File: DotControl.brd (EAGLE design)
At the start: 30.7 x 65 mm, 21 parts, among them CN1 1X4-BIG, J3 USB-MICROB, SW2 Previous, SW5 Previous, SW6 Next, SW8 Ok, U1 ATMEGA328P-MU-QFN32

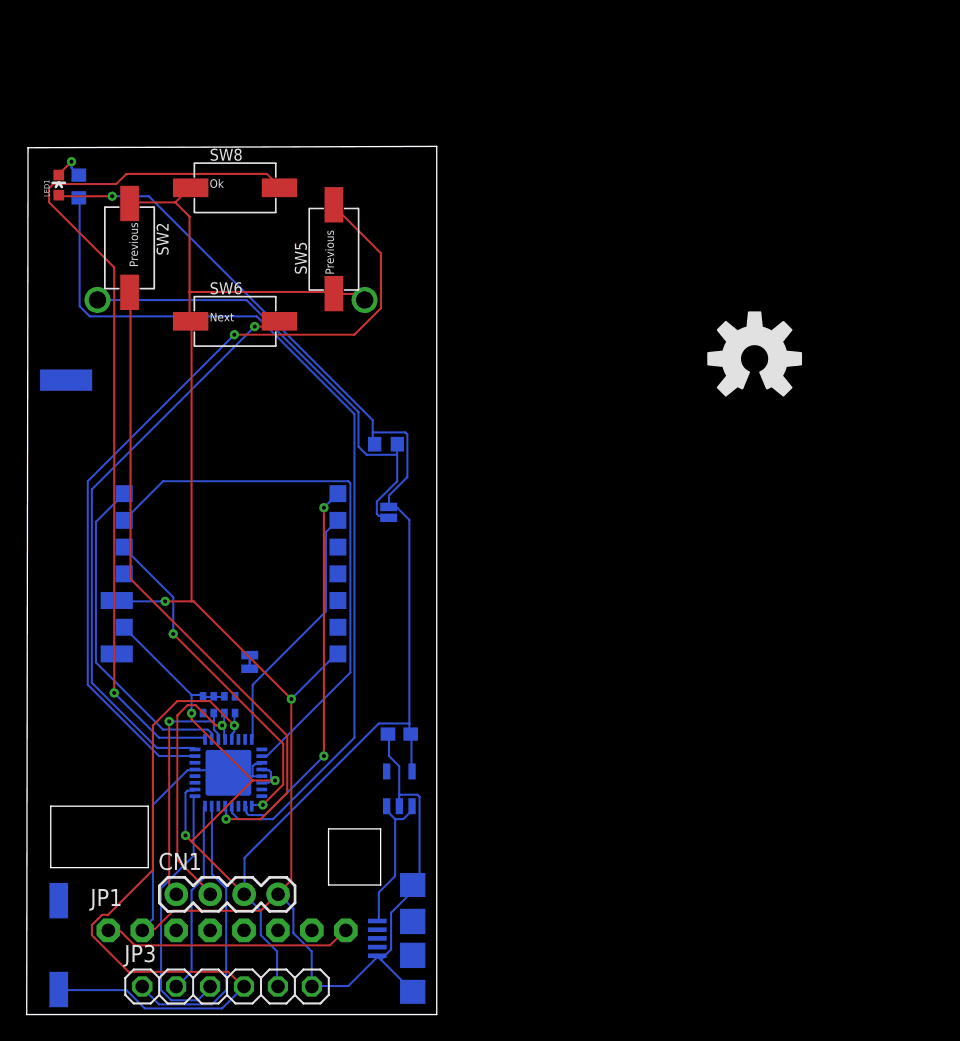
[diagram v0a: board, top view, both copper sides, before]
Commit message: Add RGB and crystal
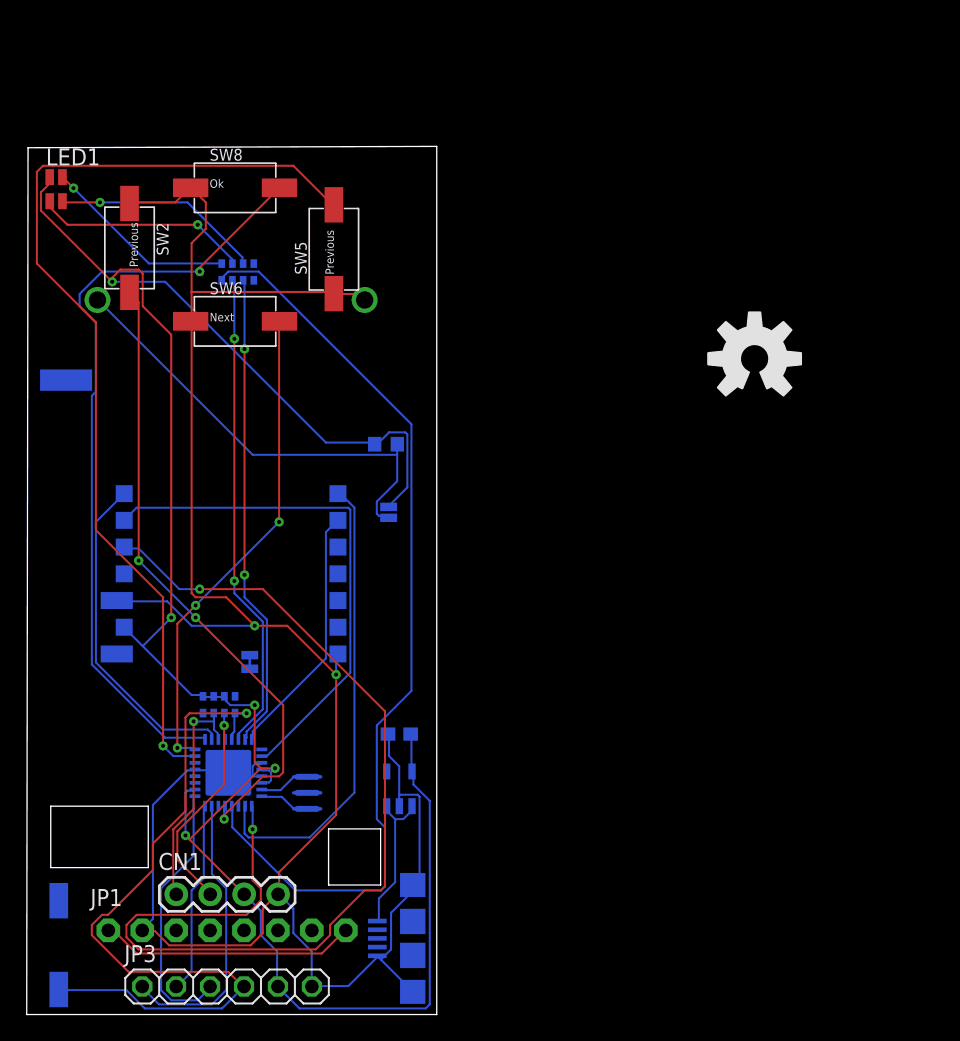
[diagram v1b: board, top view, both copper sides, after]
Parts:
- removed R1: (no value), resistor:R0603
- added R2: (no value), SparkFun:0603-ARV
- added Y1: (no value), SparkFun-Clocks:RESONATOR-SMD-3.2X1.3
- LED1: value (none) -> GM1WA55311A; device SparkFun:LED-0603 -> led:GM1WA55311A
- moved LED1 0.36 mm to (2.20, 61.8)
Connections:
- removed net N$1: LED1.C, R1.2
- new net N$10: LED1.2, R2.6
- new net N$15: LED1.1, R2.5
- new net N$6: U1.7, Y1.3
- new net N$8: U1.8, Y1.1
- new net N$9: LED1.3, R2.7
- net +3V3: now also LED1.4; no longer LED1.A
- net GND: now also Y1.2
- net LED: now also R2.4; no longer R1.1
- net RXD: now also R2.3
- net TXD: now also R2.2
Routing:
- net RSDI: track 25.7 -> 79.0 mm
- net RXD: track 0.00 -> 36.1 mm, vias 0 -> 2
- net TXD: track 0.00 -> 35.8 mm, vias 0 -> 2
- net +3V3: track 128.0 -> 156.2 mm, vias 4 -> 5
- net N$10: track 0.00 -> 16.1 mm, vias 0 -> 1
- net N$9: track 0.00 -> 15.7 mm, vias 0 -> 1
- net N$15: track 0.00 -> 14.6 mm, vias 0 -> 1
- net BUZZER: track 62.0 -> 73.2 mm
- net GND: track 155.3 -> 166.4 mm
- net MOVE_INT: track 66.2 -> 57.6 mm
- net OUTB: track 43.6 -> 36.5 mm, vias 1 -> 3
- net RSDO: track 28.3 -> 34.9 mm, vias 2 -> 0
- net SCL: track 20.9 -> 17.1 mm
- net N$6: track 0.00 -> 2.83 mm
- net RSCK: track 41.6 -> 38.8 mm
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
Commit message: Add strong GND plane
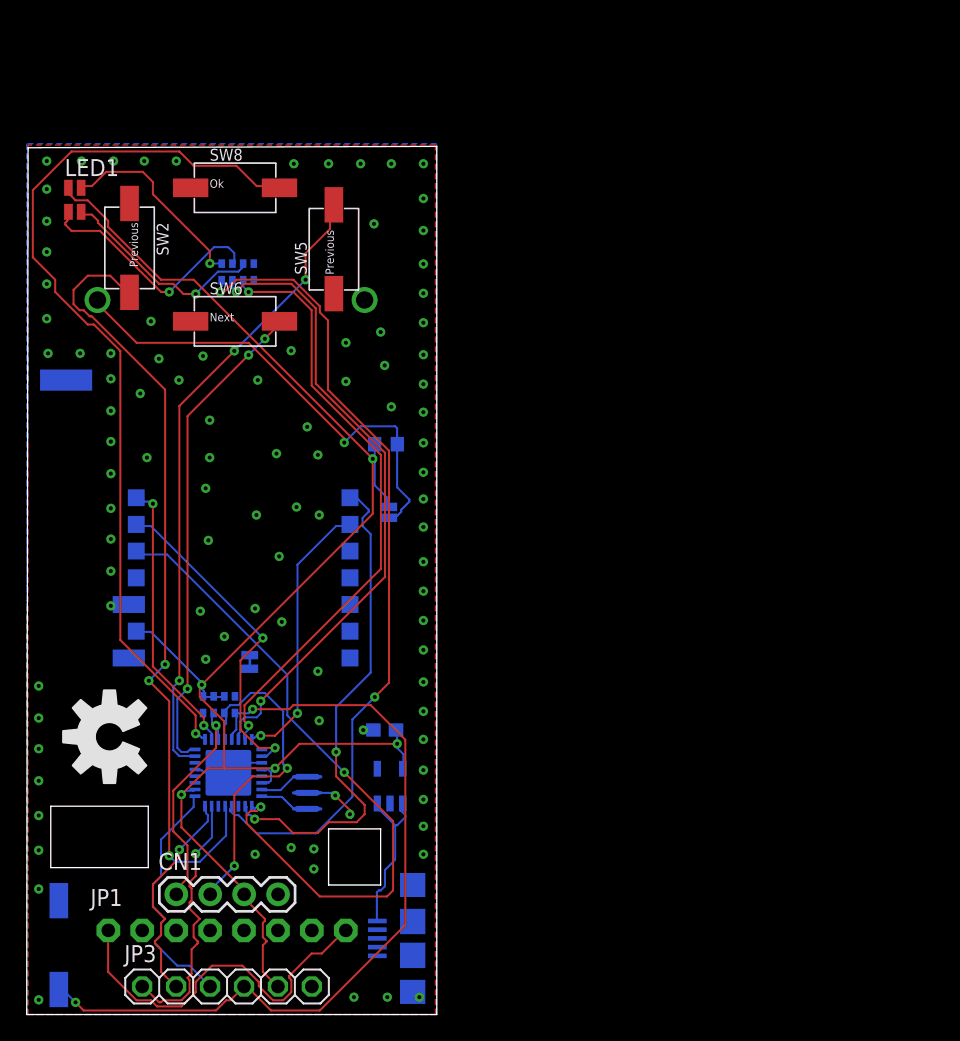
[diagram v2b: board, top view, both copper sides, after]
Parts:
- moved U$2 56.0 mm to (6.20, 20.8), turned to 90 degrees
- moved LED1 1.61 mm to (3.60, 61.0)
- moved C1 1.14 mm to (26.8, 21.3)
- moved U$1 0.95 mm to (16.7, 32.7)
- moved U$4 0.73 mm to (27.2, 17.1)
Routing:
- net GND: track 166.4 -> 12.4 mm, vias 2 -> 99
- net +3V3: track 156.2 -> 118.4 mm
- net RSDI: track 79.0 -> 50.8 mm
- net BUZZER: track 73.2 -> 47.6 mm, vias 1 -> 3
- net RSCK: track 38.8 -> 25.0 mm, vias 0 -> 2
- net ADCENA: track 47.7 -> 59.4 mm
- net RXD: track 36.1 -> 47.5 mm
- net MOVE_INT: track 57.6 -> 67.7 mm
- net TXD: track 35.8 -> 45.1 mm
- net LED: track 70.3 -> 61.0 mm, vias 0 -> 2
- net VCC: track 19.2 -> 28.0 mm
- net SCL: track 17.1 -> 25.2 mm, vias 1 -> 2
- net RST: track 55.2 -> 60.8 mm, vias 1 -> 2
- net RSEL: track 24.8 -> 21.0 mm, vias 0 -> 2
- net RSDO: track 34.9 -> 37.7 mm, vias 0 -> 2
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- added copper zone on layer 1, net GND
- added copper zone on layer 16, net GND

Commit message: Checkpoint
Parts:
- moved SW8 0.72 mm to (15.7, 62.6)
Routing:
- net GND: vias 99 -> 98

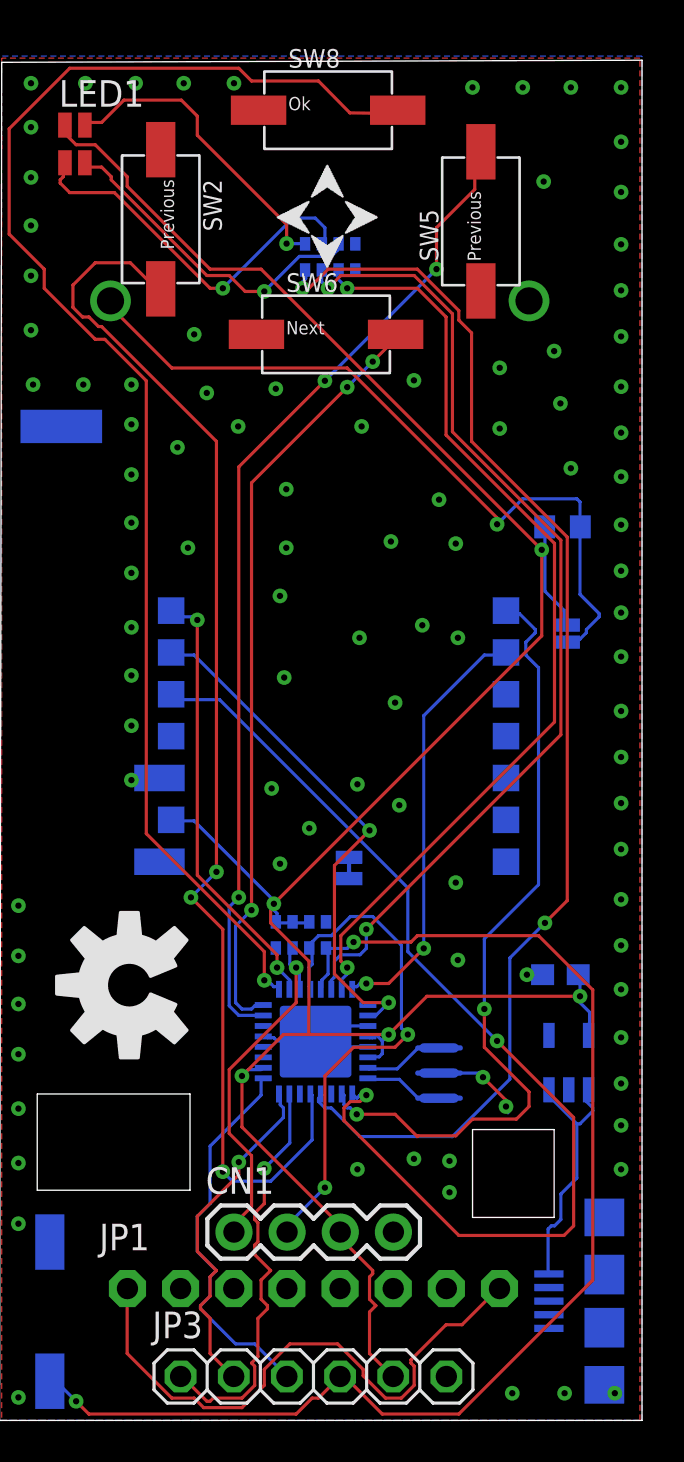
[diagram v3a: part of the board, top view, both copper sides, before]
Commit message: Add charging led
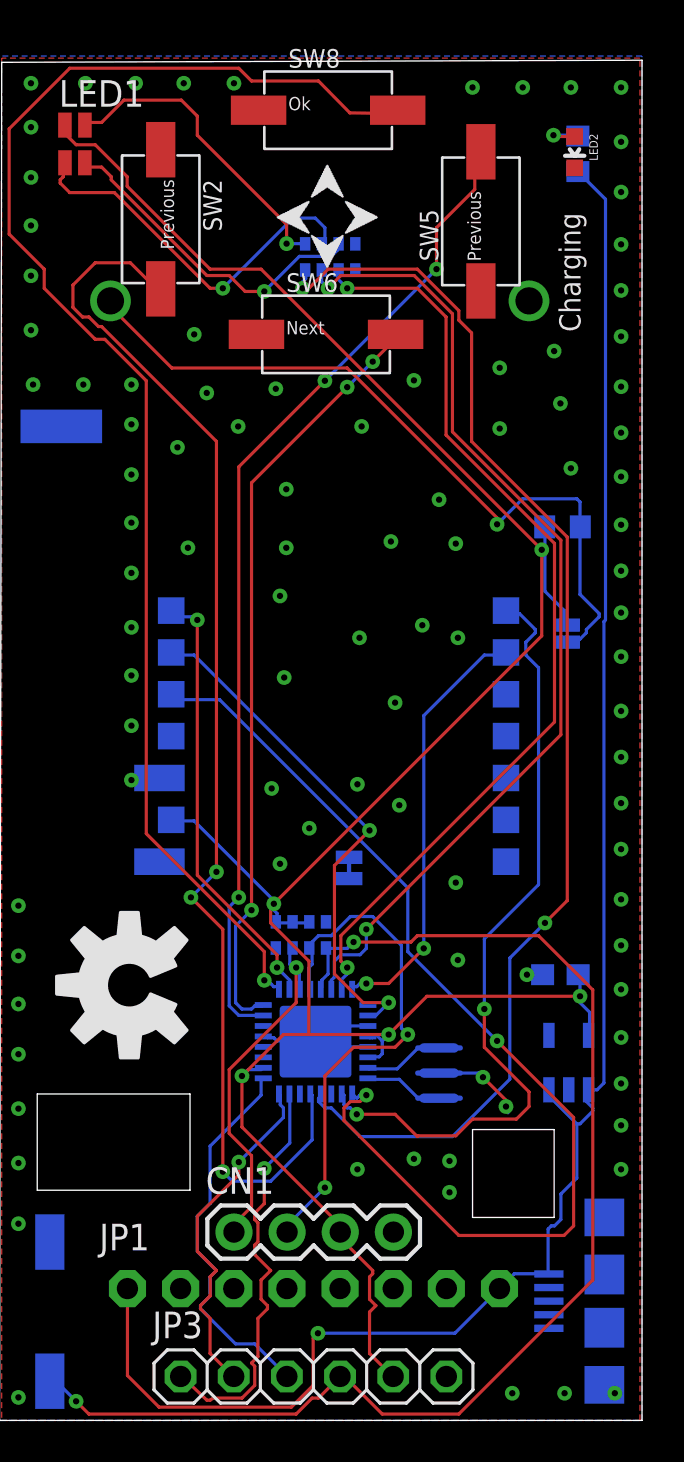
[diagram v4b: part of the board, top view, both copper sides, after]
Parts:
- added LED2: (no value), SparkFun:LED-0603
- added R1: (no value), resistor:R0603
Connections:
- removed net VCC: JP1.1, JP1.8
- new net N$1: LED2.A, R1.1
- net +5V: now also JP1.1, JP1.8, R1.2
- net GND: now also LED2.C
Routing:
- net +5V: track 12.2 -> 86.1 mm, vias 0 -> 1
- net VCC: track 28.0 -> 0.00 mm
- net N$1: track 0.00 -> 2.23 mm, vias 0 -> 1
- net GND: vias 98 -> 97
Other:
- board text added: "Charging"
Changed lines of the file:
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@@
 <setting verticaltext="up"/>
 </settings>
-<grid distance="1" unitdist="mil" unit="mil" style="lines" multiple="1" display="yes" altdistance="0.025" altunitdist="inch" altunit="inch"/>
+<grid distance="1" unitdist="mil" unit="mm" style="lines" multiple="1" display="yes" altdistance="0.025" altunitdist="inch" altunit="inch"/>
 <layers>
 <layer number="1" name="Top" color="4" fill="1" visible="yes" active="yes"/>
@@
 <layer number="23" name="tOrigins" color="15" fill="1" visible="yes" active="yes"/>
 <layer number="24" name="bOrigins" color="15" fill="1" visible="yes" active="yes"/>
-<layer number="25" name="tNames" color="7" fill="1" visible="yes" active="yes"/>
-<layer number="26" name="bNames" color="7" fill="1" visible="yes" active="yes"/>
+<layer number="25" name="tNames" color="7" fill="1" visible="no" active="yes"/>
+<layer number="26" name="bNames" color="7" fill="1" visible="no" active="yes"/>
 <layer number="27" name="tValues" color="7" fill="1" visible="no" active="yes"/>
 <layer number="28" name="bValues" color="7" fill="1" visible="no" active="yes"/>
@@
 <layer number="155" name="FabDoc3" color="7" fill="15" visible="no" active="no"/>
 <layer number="199" name="Contour" color="7" fill="1" visible="no" active="yes"/>
-<layer number="200" name="200bmp" color="1" fill="10" visible="yes" active="yes"/>
+<layer number="200" name="200bmp" color="1" fill="10" visible="no" active="yes"/>
 <layer number="201" name="201bmp" color="2" fill="1" visible="no" active="no"/>
 <layer number="202" name="202bmp" color="3" fill="1" visible="no" active="no"/>
@@
 <rectangle x1="15.6083" y1="59.9567" x2="15.7099" y2="59.9821" layer="21"/>
 <rectangle x1="15.6337" y1="59.9821" x2="15.6845" y2="60.0075" layer="21"/>
+<text x="27.7622" y="52.0192" size="1.016" layer="21" font="vector" rot="R90">Charging</text>
 </plain>
 <attributes>
@@
 <element name="JP2" library="SparkFun-Jumpers" package="SMT-JUMPER_2_NO_SILK" value="JUMPER-SMT_2_NO_SILK" x="27.1" y="37.6" rot="MR90"/>
 <element name="SJ1" library="SparkFun" package="SJ_2S-TRACE" value="SOLDERJUMPERTRACE" x="16.7" y="26.4" rot="MR90"/>
+<element name="R1" library="resistor" package="R0603" value="" x="27.6352" y="60.5282" rot="MR270"/>
+<element name="LED2" library="SparkFun" package="LED-0603" value="" x="27.4828" y="60.6044" rot="R180"/>
 </elements>
 <signals>
@@
 <via x="9.3" y="51.9" extent="1-16" drill="0.3"/>
 <via x="19.8" y="49.7" extent="1-16" drill="0.3"/>
-<via x="26" y="59.2" extent="1-16" drill="0.3"/>
 <wire x1="23.1" y1="16.4" x2="24.2" y2="15.3" width="0.1524" layer="1"/>
 <wire x1="24.2" y1="15.3" x2="24.2" y2="15" width="0.1524" layer="1"/>
@@
 <via x="21.5" y="12.4" extent="1-16" drill="0.3"/>
 <via x="17.1" y="12" extent="1-16" drill="0.3"/>
-</signal>
-<signal name="VCC">
-<contactref element="JP1" pad="1"/>
-<contactref element="JP1" pad="8"/>
-<wire x1="6.096" y1="3.2004" x2="6.096" y2="6.2484" width="0.1524" layer="1"/>
-<wire x1="8.2296" y1="1.0668" x2="6.096" y2="3.2004" width="0.1524" layer="1"/>
-<wire x1="9.2964" y1="1.0668" x2="8.2296" y2="1.0668" width="0.1524" layer="1"/>
-<wire x1="9.7536" y1="0.6096" x2="9.2964" y2="1.0668" width="0.1524" layer="1"/>
-<wire x1="11.5824" y1="0.6096" x2="9.7536" y2="0.6096" width="0.1524" layer="1"/>
-<wire x1="12.6492" y1="1.6764" x2="11.5824" y2="0.6096" width="0.1524" layer="1"/>
-<wire x1="12.6492" y1="2.4384" x2="12.6492" y2="1.6764" width="0.1524" layer="1"/>
-<wire x1="13.8684" y1="3.6576" x2="12.6492" y2="2.4384" width="0.1524" layer="1"/>
-<wire x1="16.1544" y1="3.6576" x2="13.8684" y2="3.6576" width="0.1524" layer="1"/>
-<wire x1="17.3736" y1="2.4384" x2="16.1544" y2="3.6576" width="0.1524" layer="1"/>
-<wire x1="17.3736" y1="2.1336" x2="17.3736" y2="2.4384" width="0.1524" layer="1"/>
-<wire x1="18.4404" y1="1.0668" x2="17.3736" y2="2.1336" width="0.1524" layer="1"/>
-<wire x1="19.2024" y1="1.0668" x2="18.4404" y2="1.0668" width="0.1524" layer="1"/>
-<wire x1="19.812" y1="1.6764" x2="19.2024" y2="1.0668" width="0.1524" layer="1"/>
-<wire x1="19.812" y1="2.5908" x2="19.812" y2="1.6764" width="0.1524" layer="1"/>
-<wire x1="19.6596" y1="2.7432" x2="19.812" y2="2.5908" width="0.1524" layer="1"/>
-<wire x1="19.6596" y1="2.8956" x2="19.6596" y2="2.7432" width="0.1524" layer="1"/>
-<wire x1="21.336" y1="4.572" x2="19.6596" y2="2.8956" width="0.1524" layer="1"/>
-<wire x1="22.098" y1="4.572" x2="21.336" y2="4.572" width="0.1524" layer="1"/>
-<wire x1="23.7744" y1="6.2484" x2="22.098" y2="4.572" width="0.1524" layer="1"/>
-<wire x1="6.096" y1="6.2484" x2="6.11" y2="6.3" width="0.1524" layer="1"/>
-<wire x1="23.7744" y1="6.2484" x2="23.89" y2="6.3" width="0.1524" layer="1"/>
+<contactref element="LED2" pad="C"/>
 </signal>
 <signal name="SCK">
@@
 <wire x1="27.5844" y1="14.1732" x2="27.5844" y2="11.5824" width="0.1524" layer="16"/>
 <wire x1="26.2128" y1="7.0104" x2="26.25" y2="7" width="0.1524" layer="16"/>
+<contactref element="JP1" pad="8"/>
+<contactref element="JP1" pad="1"/>
+<wire x1="6.11" y1="6.3" x2="6.11" y2="2.145" width="0.1524" layer="1"/>
+<wire x1="6.11" y1="2.145" x2="7.62" y2="0.635" width="0.1524" layer="1"/>
+<wire x1="7.62" y1="0.635" x2="13.9446" y2="0.635" width="0.1524" layer="1"/>
+<wire x1="13.9446" y1="0.635" x2="14.986" y2="1.6764" width="0.1524" layer="1"/>
+<wire x1="14.986" y1="1.6764" x2="14.986" y2="3.937" width="0.1524" layer="1"/>
+<wire x1="14.986" y1="3.937" x2="15.2146" y2="4.1656" width="0.1524" layer="1"/>
+<via x="15.2146" y="4.1656" extent="1-16" drill="0.3"/>
+<wire x1="15.2146" y1="4.1656" x2="21.7556" y2="4.1656" width="0.1524" layer="16"/>
+<wire x1="21.7556" y1="4.1656" x2="23.89" y2="6.3" width="0.1524" layer="16"/>
+<wire x1="26.2128" y1="7.0104" x2="24.6004" y2="7.0104" width="0.1524" layer="16"/>
+<wire x1="24.6004" y1="7.0104" x2="23.89" y2="6.3" width="0.1524" layer="16"/>
+<contactref element="R1" pad="2"/>
+<wire x1="28.15" y1="15.7999" x2="28.5507" y2="15.7999" width="0.1524" layer="16"/>
+<wire x1="28.5507" y1="15.7999" x2="28.8798" y2="16.129" width="0.1524" layer="16"/>
+<wire x1="28.8798" y1="16.129" x2="28.8798" y2="38.1762" width="0.1524" layer="16"/>
+<wire x1="28.8798" y1="38.1762" x2="28.956" y2="38.2524" width="0.1524" layer="16"/>
+<wire x1="28.956" y1="38.2524" x2="28.956" y2="58.3574" width="0.1524" layer="16"/>
+<wire x1="28.956" y1="58.3574" x2="27.6352" y2="59.6782" width="0.1524" layer="16"/>
 </signal>
 <signal name="MOSI">
@@
 <wire x1="11.5824" y1="1.0668" x2="12.192" y2="1.6764" width="0.1524" layer="1"/>
 <wire x1="10.2108" y1="1.0668" x2="11.5824" y2="1.0668" width="0.1524" layer="1"/>
-<wire x1="10.0584" y1="0.9144" x2="10.2108" y2="1.0668" width="0.1524" layer="1"/>
-<wire x1="9.906" y1="0.9144" x2="10.0584" y2="0.9144" width="0.1524" layer="1"/>
-<wire x1="8.6868" y1="2.1336" x2="9.906" y2="0.9144" width="0.1524" layer="1"/>
+<wire x1="10.0584" y1="0.9652" x2="10.2108" y2="1.0668" width="0.1524" layer="1"/>
+<wire x1="9.906" y1="0.9652" x2="10.0584" y2="0.9652" width="0.1524" layer="1"/>
+<wire x1="8.6868" y1="2.1336" x2="9.906" y2="0.9652" width="0.1524" layer="1"/>
 <wire x1="13.8684" y1="15.5448" x2="13.85" y2="15.6" width="0.1524" layer="16"/>
 <wire x1="8.6868" y1="2.1336" x2="8.65" y2="2.1" width="0.1524" layer="1"/>
@@
 <wire x1="15.6" y1="23.825" x2="16.7" y2="25.892" width="0" layer="19" extent="16-16"/>
 </signal>
+<signal name="N$1">
+<contactref element="R1" pad="1"/>
+<contactref element="LED2" pad="A"/>
+<wire x1="27.4828" y1="61.3544" x2="26.5296" y2="61.3544" width="0.1524" layer="1"/>
+<wire x1="26.5296" y1="61.3544" x2="26.4668" y2="61.4172" width="0.1524" layer="1"/>
+<via x="26.4668" y="61.4172" extent="1-16" drill="0.3"/>
+<wire x1="26.4668" y1="61.4172" x2="27.5962" y2="61.4172" width="0.1524" layer="16"/>
+<wire x1="27.5962" y1="61.4172" x2="27.6352" y2="61.3782" width="0.1524" layer="16"/>
+</signal>
 </signals>
+<errors>
+</errors>
 </board>
 </drawing>
